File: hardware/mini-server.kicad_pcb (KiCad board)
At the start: 2 copper layers, 1 part

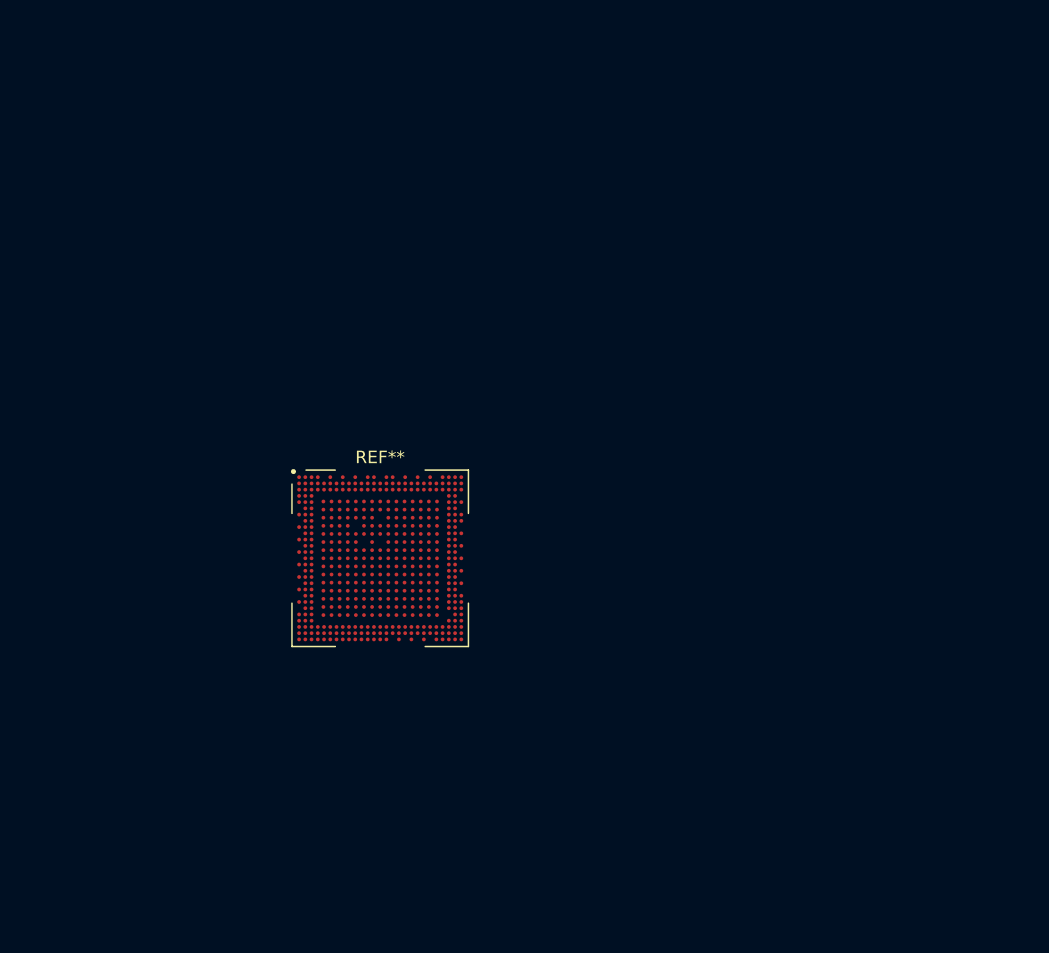
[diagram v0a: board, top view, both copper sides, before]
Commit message: Made a new power schematic and a new DDR4 ram schematic
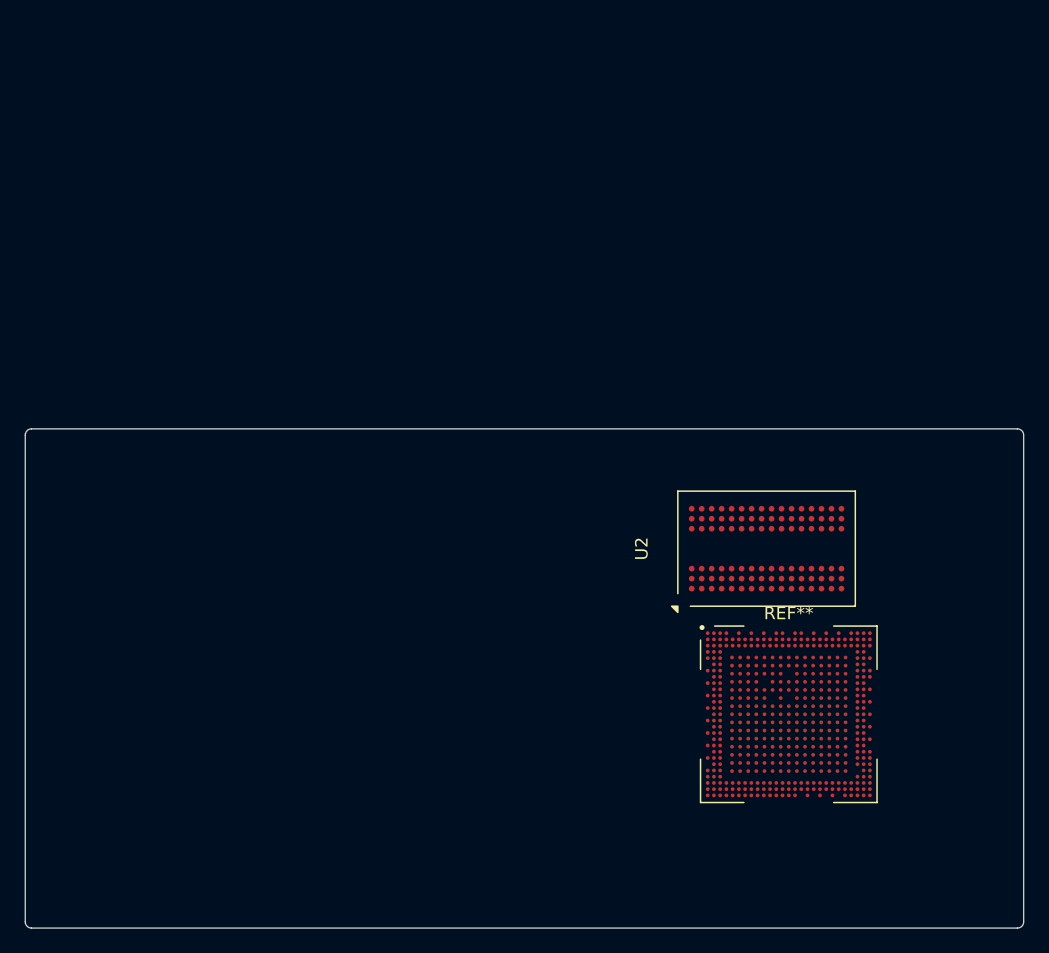
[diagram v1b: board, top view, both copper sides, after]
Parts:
- added U2: FJBD4N8GT6L9-SKC, easyeda2kicad:FBGA-96_L14.0-W9.0-R16-C6-P0.80-TL, F.Cu at (159.4, 89.1)
- U1: value ~ -> RK3562
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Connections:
- net Net-(U1-PMUPLL_AVSS) renamed GND
- U1 pad 1A1: (no net) -> unconnected-(U1D-DDR_DQS1P_A/DDR4_DQSU_P_A/LPDDR4_DQS1P_A/DDR3_DQS1P/LPDDR3_DQS1P-Pad1A1)
- U1 pad 1A10: (no net) -> unconnected-(U1D-AC4/DDR4_A4/LPDDR4_A3_B/DDR3_BA1-Pad1A10)
- U1 pad 1A13: (no net) -> unconnected-(U1D-DDR_DQS0P_B/DDR4_DQSU_P_B/LPDDR4_DQS0P_B/DDR3_DQS2P/LPDDR3_DQS2P-Pad1A13)
- U1 pad 1A15: (no net) -> unconnected-(U1D-DDR_DQS1P_B/DDR4_DQSL_P_B/LPDDR4_DQS1P_B/DDR3_DQS3P/LPDDR3_DQS0P-Pad1A15)
- U1 pad 1A3: (no net) -> unconnected-(U1D-DDR_DQS0P_A/DDR4_DQSL_P_A/LPDDR4_DQS0P_A/DDR3_DQS0P/LPDDR3_DQS3P-Pad1A3)
- U1 pad 1A6: (no net) -> unconnected-(U1D-AC12/DDR4_A12/LPDDR4_A3_A/DDR3_BA0-Pad1A6)
- U1 pad 1A7: (no net) -> unconnected-(U1D-AC16/DDR4_A16_RASN/LPDDR4_A5_A/DDR3_RASN-Pad1A7)
- U1 pad 1A8: (no net) -> unconnected-(U1D-AC5/DDR4_A5/LPDDR4_A5_B/DDR3_A11-Pad1A8)
- U1 pad 1A9: (no net) -> unconnected-(U1D-AC19/DDR4_BA1/LPDDR4_A4_B/DDR3_A12-Pad1A9)
- U1 pad 1B1: (no net) -> unconnected-(U1D-DDR_DQS1N_A/DDR4_DQSU_N_A/LPDDR4_DQS1N_A/DDR3_DQS1N/LPDDR3_DQS1N-Pad1B1)
- U1 pad 1B10: (no net) -> unconnected-(U1D-AC20/DDR4_BG0/LPDDR4_ODT1_CA_B/DDR3_WEN-Pad1B10)
- U1 pad 1B11: (no net) -> unconnected-(U1D-AC29/DDR4_RESETN/LPDDR4_RESETN/DDR3_RESETN-Pad1B11)
- U1 pad 1B13: (no net) -> unconnected-(U1D-DDR_DQS0N_B/DDR4_DQSU_N_B/LPDDR4_DQS0N_B/DDR3_DQS2N/LPDDR3_DQS2N-Pad1B13)
- U1 pad 1B15: (no net) -> unconnected-(U1D-DDR_DQS1N_B/DDR4_DQSL_N_B/LPDDR4_DQS1N_B/DDR3_DQS3N/LPDDR3_DQS0N-Pad1B15)
- U1 pad 1B3: (no net) -> unconnected-(U1D-DDR_DQS0N_A/DDR4_DQSL_N_A/LPDDR4_DQS0N_A/DDR3_DQS0N/LPDDR3_DQS3N-Pad1B3)
- U1 pad 1B6: (no net) -> unconnected-(U1D-AC1/DDR4_A1/DDR3_A2-Pad1B6)
- U1 pad 1B7: (no net) -> unconnected-(U1D-AC21/DDR4_BG1/LPDDR4_ODT1_CA_A/DDR3_BA2-Pad1B7)
- U1 pad 1B8: (no net) -> unconnected-(U1D-AC14/DDR4_A14_WEN/LPDDR4_A4_A/DDR3_A15-Pad1B8)
- U1 pad 1C9: (no net) -> unconnected-(U1D-DDR_VREFOUT-Pad1C9)
- U1 pad 1D11: (no net) -> +1V2
- U1 pad 1D4: (no net) -> unconnected-(U1D-DDR_RZQ-Pad1D4)
- U1 pad 1D6: (no net) -> +1V2
- U1 pad 1E1: (no net) -> unconnected-(U1A-SARADC1_IN7-Pad1E1)
- U1 pad 1E10: (no net) -> +1V2
- U1 pad 1E12: (no net) -> +0V9
- U1 pad 1E14: (no net) -> +1V8
- U1 pad 1E15: (no net) -> +1V8
- U1 pad 1E3: (no net) -> +1V2
- U1 pad 1E4: (no net) -> +1V2
- U1 pad 1E5: (no net) -> +1V2
- U1 pad 1E6: (no net) -> +1V2
- U1 pad 1E7: (no net) -> +1V2
- U1 pad 1E8: (no net) -> +1V2
- U1 pad 1E9: (no net) -> +1V2
- U1 pad 1F1: (no net) -> unconnected-(U1A-SARADC1_IN0-Pad1F1)
- U1 pad 1F11: (no net) -> +0V9
- U1 pad 1F12: (no net) -> +0V9
- U1 pad 1F13: (no net) -> +0V9
- U1 pad 1F14: (no net) -> unconnected-(U1E-VCCIO2-Pad1F14)
- U1 pad 1F2: (no net) -> unconnected-(U1A-SARADC1_IN2-Pad1F2)
- U1 pad 1G1: (no net) -> +1V8
- U1 pad 1G10: (no net) -> +0V9
- U1 pad 1G11: (no net) -> +0V9
- U1 pad 1G12: (no net) -> +0V9
- U1 pad 1G15: (no net) -> unconnected-(U1E-VCCIO3-Pad1G15)
- U1 pad 1G3: (no net) -> +0V9
- U1 pad 1G4: (no net) -> +0V9
- U1 pad 1G5: (no net) -> +0V9
- U1 pad 1G8: (no net) -> +0V9
- U1 pad 1H1: (no net) -> unconnected-(U1A-SARADC1_IN4-Pad1H1)
- U1 pad 1H10: (no net) -> +0V9
- U1 pad 1H11: (no net) -> +0V9
- U1 pad 1H14: (no net) -> unconnected-(U1E-VCCIO4-Pad1H14)
- U1 pad 1H15: (no net) -> unconnected-(U1C-I2S2_SDO_M0/RGMII_RXD1_M1/UART4_RTSN_M1/SPI2_MOSI_M1/PWM14_M1/RMII_RXD1/GPIO1_D7_d-Pad1H15)
- U1 pad 1H3: (no net) -> +0V9
- U1 pad 1H4: (no net) -> +0V9
- U1 pad 1H6: (no net) -> +0V9
- U1 pad 1H7: (no net) -> +0V9
- U1 pad 1H8: (no net) -> +0V9
- U1 pad 1J1: (no net) -> unconnected-(U1A-SARADC1_IN1-Pad1J1)
- U1 pad 1J10: (no net) -> +0V9
- U1 pad 1J11: (no net) -> +0V9
- U1 pad 1J12: (no net) -> +0V9
- U1 pad 1J14: (no net) -> unconnected-(U1B-SDMMC1_PWREN/RGMII_MDC_M1/PWM2_M1/I2C5_SCL_M1/RMII_MDC/GPIO1_C7_d-Pad1J14)
- U1 pad 1J15: (no net) -> unconnected-(U1C-I2S2_SDI_M0/RGMII_RXER_M1/UART4_CTSN_M1/SPI2_MISO_M1/PWM15_M1/RMII_RXER/GPIO2_A0_d-Pad1J15)
- U1 pad 1J2: (no net) -> unconnected-(U1A-SARADC1_IN3-Pad1J2)
- U1 pad 1J6: (no net) -> +0V9
- U1 pad 1J7: (no net) -> +0V9
- U1 pad 1K1: (no net) -> unconnected-(U1A-SARADC1_IN6-Pad1K1)
- U1 pad 1K10: (no net) -> +0V9
- U1 pad 1K14: (no net) -> +0V9
- U1 pad 1K15: (no net) -> +1V8
- U1 pad 1K2: (no net) -> +1V8
- U1 pad 1K3: (no net) -> unconnected-(U1E-VCCIO5-Pad1K3)
- U1 pad 1L1: (no net) -> unconnected-(U1C-I2C3_SDA_M0/UART2_RX_M1/SPDIF_TX_M0/UART5_RTSN_M1/GPIO3_A1_d-Pad1L1)
- U1 pad 1L11: (no net) -> +1V8
- U1 pad 1L12: (no net) -> unconnected-(U1A-PMUIO0-Pad1L12)
- U1 pad 1L13: (no net) -> +1V8
- U1 pad 1L14: (no net) -> +0V9
- U1 pad 1L2: (no net) -> unconnected-(U1A-SARADC1_IN5-Pad1L2)
- U1 pad 1L3: (no net) -> unconnected-(U1E-VCCIO1-Pad1L3)
- U1 pad 1L5: (no net) -> unconnected-(U1E-VCCIO6_2-Pad1L5)
- U1 pad 1L6: (no net) -> +0V9
- U1 pad 1L8: (no net) -> +0V9
- U1 pad 1M1: (no net) -> unconnected-(U1C-I2C3_SCL_M0/UART2_TX_M1/PDM_SDI3_M0/UART5_CTSN_M1/GPIO3_A0_d-Pad1M1)
- U1 pad 1M10: (no net) -> +0V9
- U1 pad 1M11: (no net) -> +0V9
- U1 pad 1M13: (no net) -> +0V9
- U1 pad 1M14: (no net) -> +3V3
- U1 pad 1M15: (no net) -> +1V8
- U1 pad 1M2: (no net) -> unconnected-(U1C-I2S0_SDO3_M0/I2S0_SDI1_M0/PDM_SDI1_M0/PCIE20_PERSTN_M1/GPIO3_B0_d-Pad1M2)
- U1 pad 1M4: (no net) -> unconnected-(U1E-VCCIO6_1-Pad1M4)
- U1 pad 1M7: (no net) -> +1V8
- U1 pad 1M8: (no net) -> +1V8
- U1 pad 1M9: (no net) -> +0V9
- U1 pad 1N9: (no net) -> +1V8
- U1 pad 1P12: (no net) -> unconnected-(U1A-nPOR-Pad1P12)
- U1 pad 1P14: (no net) -> unconnected-(U1A-USB30_OTG0_VBUSDET-Pad1P14)
- U1 pad 1P15: (no net) -> unconnected-(U1A-USB30_OTG0_ID-Pad1P15)
- U1 pad 1P3: (no net) -> unconnected-(U1C-MIPI_CSI_RX1_CLK1P-Pad1P3)
- U1 pad 1P7: (no net) -> unconnected-(U1C-MIPI_CSI_RX0_CLK1P-Pad1P7)
- U1 pad 1R11: (no net) -> unconnected-(U1A-UART2_RX_M0/PWM6_M0/NPU_AVS/GPIO0_C1_d-Pad1R11)
- U1 pad 1R13: (no net) -> unconnected-(U1A-TSADC_SHUT_M0/TSADC_SHUT_ORG/GPIO0_A1_z-Pad1R13)
- U1 pad 1R15: (no net) -> unconnected-(U1B-SDMMC0_DETN/I2C4_SDA_M1/GPIO0_A4_u-Pad1R15)
- U1 pad 1R3: (no net) -> unconnected-(U1C-MIPI_CSI_RX1_CLK1N-Pad1R3)
- U1 pad 1R7: (no net) -> unconnected-(U1C-MIPI_CSI_RX0_CLK1N-Pad1R7)
- U1 pad A10: (no net) -> unconnected-(U1D-AC2/DDR4_A2/LPDDR4_A1_A/DDR3_A4/LPDDR3_A6-PadA10)
- U1 pad A13: (no net) -> unconnected-(U1D-AC23/DDR4_CLK0P/LPDDR4_CLKN_A/DDR3_CLKP/LPDDR3_CLKP-PadA13)
- U1 pad A15: (no net) -> unconnected-(U1D-AC0/DDR4_A0/LPDDR4_CLKN_B/DDR3_A9-PadA15)
- U1 pad A18: (no net) -> unconnected-(U1D-AC6/DDR4_A6/LPDDR4_A1_B/DDR3_A14/LPDDR3_A1-PadA18)
- U1 pad A2: (no net) -> unconnected-(U1D-DDR_DM1_A/DDR4_DMU_A/LPDDR4_DM1_A/DDR3_DM1/LPDDR3_DM1-PadA2)
- U1 pad A20: (no net) -> unconnected-(U1D-DDR_DQ2_B/DDR4_DQU1_B/LPDDR4_DQ2_B/DDR3_DQ22/LPDDR3_DQ16-PadA20)
- U1 pad A22: (no net) -> unconnected-(U1D-DDR_DQ7_B/DDR4_DQU6_B/LPDDR4_DQ7_B/DDR3_DQ17/LPDDR3_DQ22-PadA22)
- U1 pad A24: (no net) -> unconnected-(U1D-DDR_DQ12_B/DDR4_DQL5_B/LPDDR4_DQ12_B/DDR3_DQ25/LPDDR3_DQ3-PadA24)
- U1 pad A25: (no net) -> unconnected-(U1D-DDR_DQ14_B/DDR4_DQL1_B/LPDDR4_DQ14_B/DDR3_DQ27/LPDDR3_DQ4-PadA25)
- U1 pad A26: (no net) -> unconnected-(U1D-DDR_DM1_B/DDR4_DML_B/LPDDR4_DM1_B/DDR3_DM3/LPDDR3_DM0-PadA26)
- U1 pad A3: (no net) -> /DDR4_PHY/DQU2
- U1 pad A4: (no net) -> /DDR4_PHY/DQU0
- U1 pad A6: (no net) -> /DDR4_PHY/DQL7
- U1 pad A8: (no net) -> /DDR4_PHY/DQL0
- U1 pad AA1: (no net) -> unconnected-(U1B-VO_LCDC_D22/RGMII_TXD0_M0/UART6_CTSN_M1/SPI1_MOSI_M0/GPIO4_A2_d-PadAA1)
- U1 pad AA2: (no net) -> unconnected-(U1B-VO_LCDC_D23/RGMII_TXD1_M0/UART6_RTSN_M1/SPI1_MISO_M0/GPIO4_A3_d-PadAA2)
- U1 pad AA25: (no net) -> unconnected-(U1A-UART1_RTSN_M0/RGMII_TXEN_M1/I2S0_SDI2_M1/PWM6_M1/RMII_TXEN/GPIO1_D3_d-PadAA25)
- U1 pad AA3: (no net) -> unconnected-(U1B-VO_LCDC_D0/RGMII_TXEN_M0/PWM13_M0/GPIO4_A4_d-PadAA3)
- U1 pad AB2: (no net) -> unconnected-(U1B-VO_LCDC_D14/RGMII_TXD3_M0/UART8_RX_M1/I2S2_SDO_M1/GPIO3_D5_d-PadAB2)
- U1 pad AB26: (no net) -> unconnected-(U1A-USB30_OTG0_SSRXP/PCIE20_RXDP-PadAB26)
- U1 pad AB27: (no net) -> unconnected-(U1A-USB30_OTG0_SSRXN/PCIE20_RXDN-PadAB27)
- U1 pad AB3: (no net) -> unconnected-(U1B-VO_LCDC_D13/RGMII_TXD2_M0/UART8_TX_M1/I2S2_SDI_M1/GPIO3_D4_d-PadAB3)
- U1 pad AC1: (no net) -> unconnected-(U1B-VO_LCDC_D2/RGMII_MDC_M0/UART9_TX_M0/GPIO4_B2_d-PadAC1)
- U1 pad AC2: (no net) -> unconnected-(U1B-VO_LCDC_D18/RGMII_MDIO_M0/UART9_RX_M0/GPIO4_B3_d-PadAC2)
- U1 pad AC26: (no net) -> unconnected-(U1A-PCIE20_REFCLKP-PadAC26)
- U1 pad AC27: (no net) -> unconnected-(U1A-PCIE20_REFCLKN-PadAC27)
- U1 pad AD1: (no net) -> unconnected-(U1C-MIPI_CSI_RX1_D3P-PadAD1)
- U1 pad AD2: (no net) -> unconnected-(U1C-MIPI_CSI_RX1_D3N-PadAD2)
- U1 pad AD26: (no net) -> unconnected-(U1A-USB30_OTG0_SSTXP/PCIE20_TXDP-PadAD26)
- U1 pad AD27: (no net) -> unconnected-(U1A-USB30_OTG0_SSTXN/PCIE20_TXDN-PadAD27)
- U1 pad AE1: (no net) -> unconnected-(U1C-MIPI_CSI_RX1_D2P-PadAE1)
- U1 pad AE15: (no net) -> unconnected-(U1C-I2C2_SDA_M0/PCIE20_WAKEN_M0/GPIO0_B6_d-PadAE15)
- U1 pad AE16: (no net) -> unconnected-(U1A-UART2_RTSN_M0/PWM0_M0/SPI0_CLK_M0/GPIO0_C3_d-PadAE16)
- U1 pad AE17: (no net) -> unconnected-(U1C-I2C1_SCL_M0/GPIO0_B3_d-PadAE17)
- U1 pad AE18: (no net) -> unconnected-(U1A-UART6_RTSN_M0/PWM2_M0/SPI0_MISO_M0/GPIO0_C5_d-PadAE18)
- U1 pad AE19: (no net) -> unconnected-(U1A-UART6_RX_M0/GPIO0_C7_d-PadAE19)
- U1 pad AE20: (no net) -> unconnected-(U1A-UART0_TX_M0/JTAG_CPU_MCU_TCK_M0/GPIO0_D1_u-PadAE20)
- U1 pad AE22: (no net) -> unconnected-(U1B-SDMMC0_PWREN/I2C4_SCL_M1/PMU_DEBUG/GPIO0_A5_d-PadAE22)
- U1 pad AE23: (no net) -> unconnected-(U1C-I2C0_SDA/GPIO0_B2_d-PadAE23)
- U1 pad AE24: (no net) -> unconnected-(U1A-REF_CLK_OUT/GPIO0_A0_d-PadAE24)
- U1 pad AE26: (no net) -> unconnected-(U1A-USB20_HOST1_DM-PadAE26)
- U1 pad AE27: (no net) -> unconnected-(U1A-USB20_HOST1_DP-PadAE27)
- U1 pad AF1: (no net) -> unconnected-(U1C-MIPI_CSI_RX1_D2N-PadAF1)
- U1 pad AF10: (no net) -> unconnected-(U1C-MIPI_DSI_TX_D3N/LVDS_TX_D3N-PadAF10)
- U1 pad AF11: (no net) -> unconnected-(U1C-MIPI_DSI_TX_D2P/LVDS_TX_D2P-PadAF11)
- U1 pad AF12: (no net) -> unconnected-(U1C-MIPI_DSI_TX_CLKN/LVDS_TX_CLKN-PadAF12)
- U1 pad AF13: (no net) -> unconnected-(U1C-MIPI_DSI_TX_D1P/LVDS_TX_D1P-PadAF13)
- U1 pad AF14: (no net) -> unconnected-(U1C-MIPI_DSI_TX_D0N/LVDS_TX_D0N-PadAF14)
- U1 pad AF15: (no net) -> unconnected-(U1A-SPI0_CSN1_M0/PWM4_M0/CPU_AVS/SPDIF_TX_M1/GPIO0_B7_d-PadAF15)
- U1 pad AF16: (no net) -> unconnected-(U1C-I2C2_SCL_M0/PCIE20_PERSTN_M0/GPIO0_B5_d-PadAF16)
- U1 pad AF17: (no net) -> unconnected-(U1A-UART2_TX_M0/PWM7_M0/GPU_AVS/GPIO0_C0_d-PadAF17)
- U1 pad AF18: (no net) -> unconnected-(U1C-I2C1_SDA_M0/GPIO0_B4_d-PadAF18)
- U1 pad AF19: (no net) -> unconnected-(U1A-UART6_TX_M0/GPIO0_C6_d-PadAF19)
- U1 pad AF2: (no net) -> unconnected-(U1C-MIPI_CSI_RX1_CLK0P-PadAF2)
- U1 pad AF20: (no net) -> unconnected-(U1A-UART0_RX_M0/JTAG_CPU_MCU_TMS_M0/GPIO0_D0_u-PadAF20)
- U1 pad AF21: (no net) -> unconnected-(U1A-CLK_32K_IN/CLK0_32K_OUT/PCIE20_BUTTONRSTN/GPIO0_B0_d-PadAF21)
- U1 pad AF22: (no net) -> unconnected-(U1A-PWR_CTRL1/GPIO0_A3_u-PadAF22)
- U1 pad AF23: (no net) -> unconnected-(U1A-PWR_CTRL0/TSADC_SHUT_M1/GPIO0_A2_d-PadAF23)
- U1 pad AF25: (no net) -> unconnected-(U1A-OSC_SOC_XOUT-PadAF25)
- U1 pad AF26: (no net) -> unconnected-(U1A-USB30_OTG0_DM-PadAF26)
- U1 pad AF27: (no net) -> unconnected-(U1A-USB30_OTG0_DP-PadAF27)
- U1 pad AF3: (no net) -> unconnected-(U1C-MIPI_CSI_RX1_D1P-PadAF3)
- U1 pad AF4: (no net) -> unconnected-(U1C-MIPI_CSI_RX1_D0P-PadAF4)
- U1 pad AF5: (no net) -> unconnected-(U1C-MIPI_CSI_RX0_D3P-PadAF5)
- U1 pad AF6: (no net) -> unconnected-(U1C-MIPI_CSI_RX0_D2P-PadAF6)
- U1 pad AF7: (no net) -> unconnected-(U1C-MIPI_CSI_RX0_CLK0P-PadAF7)
- U1 pad AF8: (no net) -> unconnected-(U1C-MIPI_CSI_RX0_D1P-PadAF8)
- U1 pad AF9: (no net) -> unconnected-(U1C-MIPI_CSI_RX0_D0P-PadAF9)
- U1 pad AG10: (no net) -> unconnected-(U1C-MIPI_DSI_TX_D3P/LVDS_TX_D3P-PadAG10)
- U1 pad AG11: (no net) -> unconnected-(U1C-MIPI_DSI_TX_D2N/LVDS_TX_D2N-PadAG11)
- U1 pad AG12: (no net) -> unconnected-(U1C-MIPI_DSI_TX_CLKP/LVDS_TX_CLKP-PadAG12)
- U1 pad AG13: (no net) -> unconnected-(U1C-MIPI_DSI_TX_D1N/LVDS_TX_D1N-PadAG13)
- U1 pad AG14: (no net) -> unconnected-(U1C-MIPI_DSI_TX_D0P/LVDS_TX_D0P-PadAG14)
- U1 pad AG17: (no net) -> unconnected-(U1A-UART2_CTSN_M0/PWM5_M0/SPI0_CSN0_M0/GPIO0_C2_d-PadAG17)
- U1 pad AG19: (no net) -> unconnected-(U1A-UART6_CTSN_M0/PWM1_M0/SPI0_MOSI_M0/GPIO0_C4_d-PadAG19)
- U1 pad AG2: (no net) -> unconnected-(U1C-MIPI_CSI_RX1_CLK0N-PadAG2)
- U1 pad AG21: (no net) -> unconnected-(U1A-PWM3_M0/GPIO0_A7_d-PadAG21)
- U1 pad AG23: (no net) -> unconnected-(U1C-I2C0_SCL/GPIO0_B1_d-PadAG23)
- U1 pad AG24: (no net) -> unconnected-(U1A-PCIE20_CLKREQN_M0/GPIO0_A6_d-PadAG24)
- U1 pad AG25: (no net) -> unconnected-(U1A-OSC_SOC_XIN-PadAG25)
- U1 pad AG3: (no net) -> unconnected-(U1C-MIPI_CSI_RX1_D1N-PadAG3)
- U1 pad AG4: (no net) -> unconnected-(U1C-MIPI_CSI_RX1_D0N-PadAG4)
- U1 pad AG5: (no net) -> unconnected-(U1C-MIPI_CSI_RX0_D3N-PadAG5)
- U1 pad AG6: (no net) -> unconnected-(U1C-MIPI_CSI_RX0_D2N-PadAG6)
- U1 pad AG7: (no net) -> unconnected-(U1C-MIPI_CSI_RX0_CLK0N-PadAG7)
- U1 pad AG8: (no net) -> unconnected-(U1C-MIPI_CSI_RX0_D1N-PadAG8)
- U1 pad AG9: (no net) -> unconnected-(U1C-MIPI_CSI_RX0_D0N-PadAG9)
- U1 pad B1: (no net) -> /DDR4_PHY/DQU3
- U1 pad B10: (no net) -> unconnected-(U1D-AC11/DDR4_A11/LPDDR4_A0_A/DDR3_A6/LPDDR3_A8-PadB10)
- U1 pad B11: (no net) -> unconnected-(U1D-AC3/DDR4_A3/LPDDR4_CS0N_A/DDR3_ODT1/LPDDR3_ODT0-PadB11)
- U1 pad B12: (no net) -> unconnected-(U1D-AC25/DDR4_CS0N/LPDDR4_CKE1_A/DDR3_A3-PadB12)
- U1 pad B13: (no net) -> unconnected-(U1D-AC24/DDR4_CLK0N/LPDDR4_CLKP_A/DDR3_CLKN/LPDDR3_CLKN-PadB13)
- U1 pad B15: (no net) -> unconnected-(U1D-AC9/DDR4_A9/LPDDR4_CLKP_B/DDR3_A13-PadB15)
- U1 pad B16: (no net) -> unconnected-(U1D-AC17/DDR4_ACTN/LPDDR4_CKE1_B/DDR3_CASN/LPDDR3_CS1N-PadB16)
- U1 pad B17: (no net) -> unconnected-(U1D-AC28/DDR4_ODT1/LPDDR4_CS0N_B/DDR3_CS0N/LPDDR3_A2-PadB17)
- U1 pad B18: (no net) -> unconnected-(U1D-AC7/DDR4_A7/LPDDR4_A0_B/DDR3_A5/LPDDR3_A0-PadB18)
- U1 pad B19: (no net) -> unconnected-(U1D-AC13/DDR4_A13/LPDDR4_ODT0_CA_B/DDR3_A8/LPDDR3_ODT1-PadB19)
- U1 pad B2: (no net) -> /DDR4_PHY/DQU7
- U1 pad B20: (no net) -> unconnected-(U1D-DDR_DQ1_B/DDR4_DQU3_B/LPDDR4_DQ1_B/DDR3_DQ20/LPDDR3_DQ21-PadB20)
- U1 pad B21: (no net) -> unconnected-(U1D-DDR_DM0_B/DDR4_DMU_B/LPDDR4_DM0_B/DDR3_DM2/LPDDR3_DM2-PadB21)
- U1 pad B22: (no net) -> unconnected-(U1D-DDR_DQ0_B/DDR4_DQU7_B/LPDDR4_DQ0_B/DDR3_DQ16/LPDDR3_DQ17-PadB22)
- U1 pad B23: (no net) -> unconnected-(U1D-DDR_DQ5_B/DDR4_DQU4_B/LPDDR4_DQ5_B/DDR3_DQ23/LPDDR3_DQ19-PadB23)
- U1 pad B24: (no net) -> unconnected-(U1D-DDR_DQ13_B/DDR4_DQL7_B/LPDDR4_DQ13_B/DDR3_DQ31/LPDDR3_DQ5-PadB24)
- U1 pad B25: (no net) -> unconnected-(U1D-DDR_DQ15_B/DDR4_DQL3_B/LPDDR4_DQ15_B/DDR3_DQ29/LPDDR3_DQ7-PadB25)
- U1 pad B26: (no net) -> unconnected-(U1D-DDR_DQ11_B/DDR4_DQL6_B/LPDDR4_DQ11_B/DDR3_DQ24/LPDDR3_DQ6-PadB26)
- U1 pad B27: (no net) -> unconnected-(U1D-DDR_DQ10_B/DDR4_DQL2_B/LPDDR4_DQ10_B/DDR3_DQ28/LPDDR3_DQ2-PadB27)
- U1 pad B3: (no net) -> /DDR4_PHY/DQU6
- U1 pad B4: (no net) -> /DDR4_PHY/DQU4
- U1 pad B5: (no net) -> /DDR4_PHY/DQL1
- U1 pad B6: (no net) -> /DDR4_PHY/DQL6
- U1 pad B7: (no net) -> unconnected-(U1D-DDR_DM0_A/DDR4_DML_A/LPDDR4_DM0_A/DDR3_DM0/LPDDR3_DM3-PadB7)
- U1 pad B8: (no net) -> /DDR4_PHY/DQL2
- U1 pad B9: (no net) -> unconnected-(U1D-AC8/DDR4_A8/LPDDR4_ODT0_CA_A/DDR3_A7/LPDDR3_A9-PadB9)
- U1 pad C1: (no net) -> /DDR4_PHY/DQU5
- U1 pad C10: (no net) -> unconnected-(U1D-AC15/DDR4_A15_CASN/LPDDR4_A2_A/DDR3_A0/LPDDR3_A7-PadC10)
- U1 pad C11: (no net) -> unconnected-(U1D-AC26/DDR4_CS1N/LPDDR4_CS1N_A/DDR3_CS1N/LPDDR3_A5-PadC11)
- U1 pad C12: (no net) -> unconnected-(U1D-AC22/DDR4_CKE0/LPDDR4_CKE0_A/DDR3_CKE/LPDDR3_CKE-PadC12)
- U1 pad C16: (no net) -> unconnected-(U1D-AC10/DDR4_A10/LPDDR4_CKE0_B/DDR3_A10/LPDDR3_CS0N-PadC16)
- U1 pad C17: (no net) -> unconnected-(U1D-AC27/DDR4_ODT0/LPDDR4_CS1N_B/DDR3_ODT0/LPDDR3_A4-PadC17)
- U1 pad C18: (no net) -> unconnected-(U1D-AC18/DDR4_BA0/LPDDR4_A2_B/DDR3_A1/LPDDR3_A3-PadC18)
- U1 pad C2: (no net) -> /DDR4_PHY/DQU1
- U1 pad C20: (no net) -> unconnected-(U1D-DDR_DQ3_B/DDR4_DQU5_B/LPDDR4_DQ3_B/DDR3_DQ18/LPDDR3_DQ20-PadC20)
- U1 pad C22: (no net) -> unconnected-(U1D-DDR_DQ6_B/DDR4_DQU2_B/LPDDR4_DQ6_B/DDR3_DQ19/LPDDR3_DQ18-PadC22)
- U1 pad C23: (no net) -> unconnected-(U1D-DDR_DQ4_B/DDR4_DQU0_B/LPDDR4_DQ4_B/DDR3_DQ21/LPDDR3_DQ23-PadC23)
- U1 pad C26: (no net) -> unconnected-(U1D-DDR_DQ8_B/DDR4_DQL0_B/LPDDR4_DQ8_B/DDR3_DQ26/LPDDR3_DQ0-PadC26)
- U1 pad C27: (no net) -> unconnected-(U1D-DDR_DQ9_B/DDR4_DQL4_B/LPDDR4_DQ9_B/DDR3_DQ30/LPDDR3_DQ1-PadC27)
- U1 pad C5: (no net) -> /DDR4_PHY/DQL5
- U1 pad C6: (no net) -> /DDR4_PHY/DQL3
- U1 pad C8: (no net) -> /DDR4_PHY/DQL4
- U1 pad D1: (no net) -> unconnected-(U1C-I2S1_SDO0_M1/CAM_CLK3_OUT/UART8_RTSN_M0/SPI0_CLK_M1/PWM13_M1/GPIO3_B5_d-PadD1)
- U1 pad D25: (no net) -> unconnected-(U1A-SARADC0_IN4-PadD25)
- U1 pad D26: (no net) -> unconnected-(U1A-SARADC0_BOOT-PadD26)
- U1 pad D3: (no net) -> unconnected-(U1C-I2C5_SDA_M0/ISP_FLASH_TRIGOUT/UART9_RX_M1/GPIO3_C3_d-PadD3)
- U1 pad E1: (no net) -> unconnected-(U1C-I2C5_SCL_M0/ISP_PRELIGHT_TRIGOUT/UART9_TX_M1/GPIO3_C2_d-PadE1)
- U1 pad E2: (no net) -> unconnected-(U1C-I2S1_SDI0_M1/ISP_FLASH_TRIGIN/UART3_RTSN_M1/GPIO3_C1_d-PadE2)
- U1 pad E25: (no net) -> unconnected-(U1A-SARADC0_IN2-PadE25)
- U1 pad E26: (no net) -> unconnected-(U1A-SARADC0_IN5-PadE26)
- U1 pad E27: (no net) -> unconnected-(U1A-SARADC0_IN6-PadE27)
- U1 pad F2: (no net) -> unconnected-(U1C-I2S1_LRCK_M1/CAM_CLK2_OUT/UART8_CTSN_M0/SPI0_MOSI_M1/PWM12_M1/GPIO3_B4_d-PadF2)
- U1 pad F25: (no net) -> unconnected-(U1A-SARADC0_IN7-PadF25)
- U1 pad F26: (no net) -> unconnected-(U1A-SARADC0_IN1-PadF26)
- U1 pad G1: (no net) -> unconnected-(U1C-I2S1_SCLK_M1/CAM_CLK1_OUT_M0/UART8_RX_M0/GPIO3_B3_d-PadG1)
- U1 pad G2: (no net) -> unconnected-(U1C-I2S1_SDO2_M1/I2S1_SDI2_M1/UART3_TX_M1/SPI0_CSN0_M1/I2C4_SDA_M0/GPIO3_B7_d-PadG2)
- U1 pad G26: (no net) -> unconnected-(U1A-SARADC0_IN3-PadG26)
- U1 pad G3: (no net) -> unconnected-(U1C-I2S1_SDO1_M1/I2S1_SDI3_M1/UART3_CTSN_M1/SPI0_CSN1_M1/I2C4_SCL_M0/GPIO3_B6_d-PadG3)
- U1 pad H2: (no net) -> unconnected-(U1C-I2S1_SDO3_M1/I2S1_SDI1_M1/UART3_RX_M1/SPI0_MISO_M1/GPIO3_C0_d-PadH2)
- U1 pad H25: (no net) -> unconnected-(U1A-EMMC_D2/FSPI_D2/GPIO1_A2_u-PadH25)
- U1 pad H26: (no net) -> unconnected-(U1A-EMMC_D6/GPIO1_A6_u-PadH26)
- U1 pad H27: (no net) -> unconnected-(U1A-EMMC_D7/GPIO1_A7_u-PadH27)
- U1 pad H3: (no net) -> unconnected-(U1C-I2S1_MCLK_M1/CAM_CLK0_OUT_M0/UART8_TX_M0/GPIO3_B2_d-PadH3)
- U1 pad J1: (no net) -> unconnected-(U1C-I2S0_SDO1_M0/I2S0_SDI3_M0/PDM_CLK0_M0/PCIE20_CLKREQN_M1/UART5_TX_M1/GPIO3_A6_d-PadJ1)
- U1 pad J2: (no net) -> unconnected-(U1C-I2S0_SDI0_M0/PDM_SDI0_M0/GPIO3_B1_d-PadJ2)
- U1 pad J25: (no net) -> unconnected-(U1A-EMMC_D0/FSPI_D0/GPIO1_A0_u-PadJ25)
- U1 pad J26: (no net) -> unconnected-(U1A-EMMC_D1/FSPI_D1/GPIO1_A1_u-PadJ26)
- U1 pad K2: (no net) -> unconnected-(U1C-I2S0_MCLK_M0/UART2_CTSN_M1/PDM_CLK1_M0/GPIO3_A2_d-PadK2)
- U1 pad K25: (no net) -> unconnected-(U1A-EMMC_D5/GPIO1_A5_u-PadK25)
- U1 pad K26: (no net) -> unconnected-(U1A-EMMC_D4/GPIO1_A4_u-PadK26)
- U1 pad K27: (no net) -> unconnected-(U1A-EMMC_D3/FSPI_D3/GPIO1_A3_u-PadK27)
- U1 pad K3: (no net) -> unconnected-(U1C-I2S0_SDO0_M0/PWM9_M0/GPIO3_A5_d-PadK3)
- U1 pad L1: (no net) -> unconnected-(U1C-I2S0_LRCK_M0/PWM8_M0/GPIO3_A4_d-PadL1)
- U1 pad L2: (no net) -> unconnected-(U1C-I2S0_SDO2_M0/I2S0_SDI2_M0/PDM_SDI2_M0/PCIE20_WAKEN_M1/UART5_RX_M1/GPIO3_A7_d-PadL2)
- U1 pad L26: (no net) -> unconnected-(U1A-EMMC_STRB/FSPI_CSN1/GPIO1_B2_d-PadL26)
- U1 pad L3: (no net) -> unconnected-(U1C-I2S0_SCLK_M0/UART2_RTSN_M1/GPIO3_A3_d-PadL3)
- U1 pad M2: (no net) -> unconnected-(U1B-VO_LCDC_HSYNC/I2S1_SDO1_M0/UART9_CTSN_M0/SPI2_CSN1_M0/I2C1_SCL_M1/UART3_TX_M0/GPIO4_B4_d-PadM2)
- U1 pad M25: (no net) -> unconnected-(U1A-EMMC_CLK/FSPI_CLK/GPIO1_B1_d-PadM25)
- U1 pad M26: (no net) -> unconnected-(U1A-EMMC_CMD/FSPI_CSN0/GPIO1_B0_u-PadM26)
- U1 pad M3: (no net) -> unconnected-(U1B-VO_LCDC_VSYNC/I2S1_SDO2_M0/UART9_RTSN_M0/SPI2_CSN0_M0/I2C1_SDA_M1/UART3_RX_M0/GPIO4_B5_d-PadM3)
- U1 pad N1: (no net) -> unconnected-(U1B-VO_LCDC_D3/I2S1_MCLK_M0/UART7_TX_M0/GPIO3_C4_d-PadN1)
- U1 pad N2: (no net) -> unconnected-(U1B-VO_LCDC_D4/I2S1_SCLK_M0/UART4_CTSN_M0/PWM14_M0/GPIO3_C5_d-PadN2)
- U1 pad N25: (no net) -> unconnected-(U1B-SDMMC0_D2/JTAG_CPU_MCU_TCK_M1/UART5_CTSN_M0/SPI1_CSN1_M1/PWM10_M0/DSM_AUD_RP/GPIO1_B5_u-PadN25)
- U1 pad N26: (no net) -> unconnected-(U1B-SDMMC0_D3/JTAG_CPU_MCU_TMS_M1/UART5_RTSN_M0/SPI1_CSN0_M1/PWM11_M0/DSM_AUD_RN/GPIO1_B6_u-PadN26)
- U1 pad N3: (no net) -> unconnected-(U1B-VO_LCDC_DEN/I2S1_SDO3_M0/UART3_CTSN_M0/SPI2_CLK_M0/GPIO4_B6_d-PadN3)
- U1 pad P2: (no net) -> unconnected-(U1B-VO_LCDC_D6/I2S1_SDO0_M0/UART7_RX_M0/GPIO3_C7_d-PadP2)
- U1 pad P25: (no net) -> unconnected-(U1B-SDMMC0_CMD/SPDIF_TX_M2/UART5_RX_M0/GPIO1_B7_u-PadP25)
- U1 pad P27: (no net) -> unconnected-(U1B-SDMMC0_CLK/TEST_CLK_OUT/UART5_TX_M0/SPI1_CLK_M1/GPIO1_C0_d-PadP27)
- U1 pad P3: (no net) -> unconnected-(U1B-VO_LCDC_D5/I2S1_LRCK_M0/UART4_RTSN_M0/PWM15_M0/GPIO3_C6_d-PadP3)
- U1 pad R1: (no net) -> unconnected-(U1B-VO_LCDC_D10/I2S1_SDI1_M0/UART4_RX_M0/UART3_RTSN_M0/GPIO3_D1_d-PadR1)
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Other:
- board outline added: 80 x 40 mm

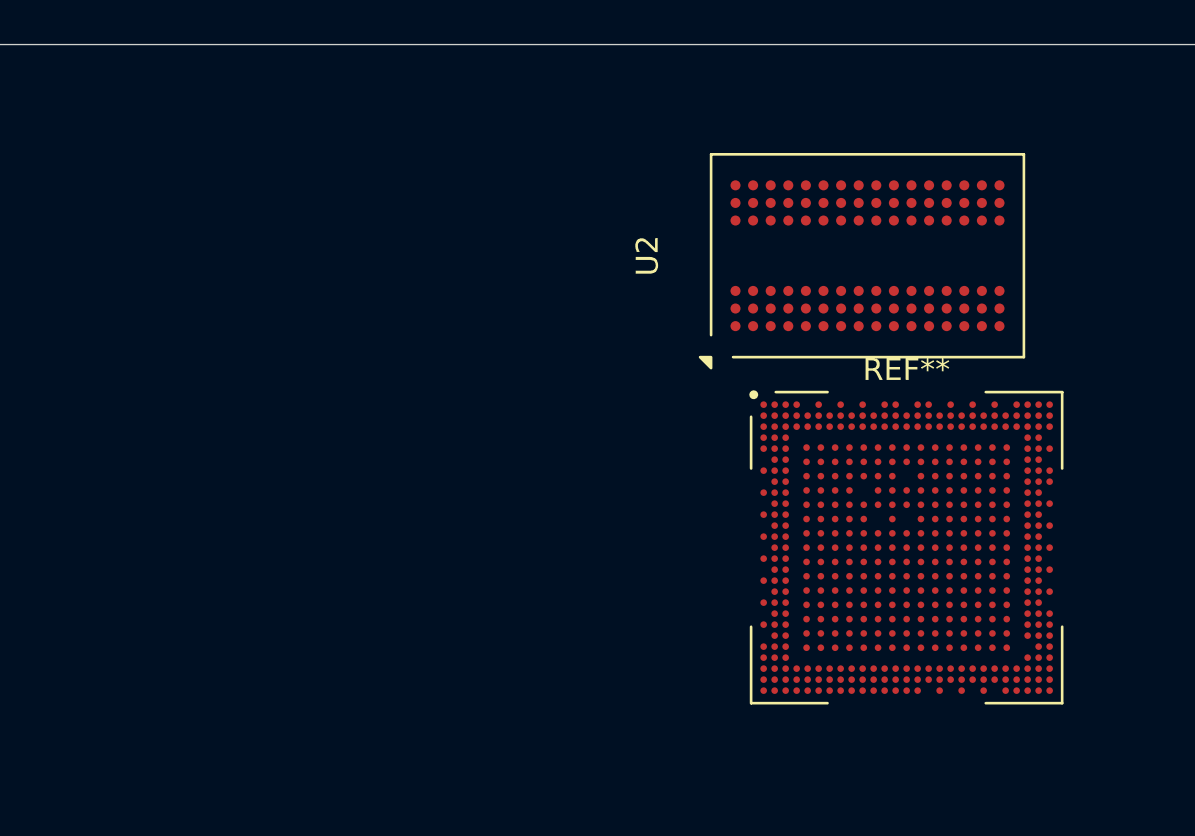
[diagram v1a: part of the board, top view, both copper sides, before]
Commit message: DDR4 schematic almost completed
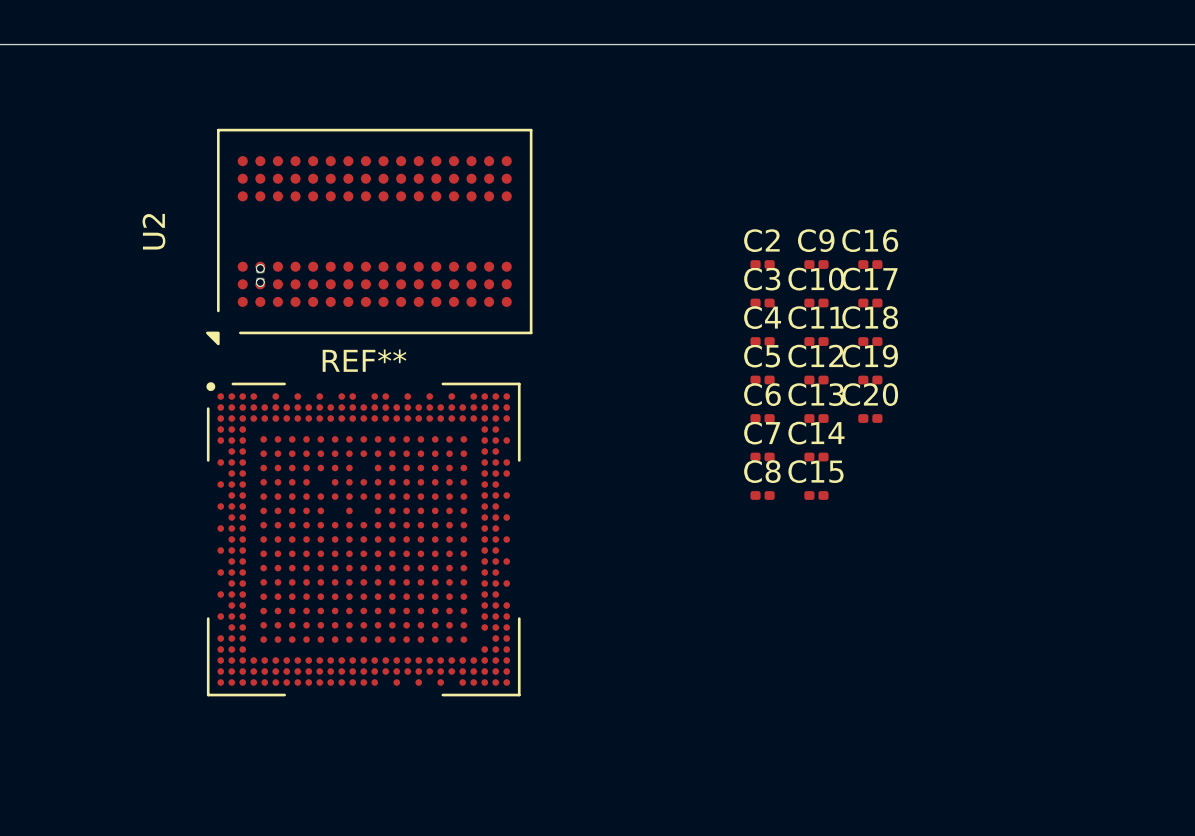
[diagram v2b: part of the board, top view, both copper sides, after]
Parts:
- added C1: 100n, Capacitor_SMD:C_0201_0603Metric, B.Cu at (131.8, 90.0)
- added C10: 100n, Capacitor_SMD:C_0201_0603Metric, F.Cu at (157.1, 91.2)
- added C11: 100n, Capacitor_SMD:C_0201_0603Metric, F.Cu at (157.1, 93.0)
- added C12: 100n, Capacitor_SMD:C_0201_0603Metric, F.Cu at (157.1, 94.8)
- added C13: 100n, Capacitor_SMD:C_0201_0603Metric, F.Cu at (157.1, 96.5)
- added C14: 100n, Capacitor_SMD:C_0201_0603Metric, F.Cu at (157.1, 98.2)
- added C15: 100n, Capacitor_SMD:C_0201_0603Metric, F.Cu at (157.1, 100.0)
- added C16: 100n, Capacitor_SMD:C_0201_0603Metric, F.Cu at (159.5, 89.5)
- added C17: 100n, Capacitor_SMD:C_0201_0603Metric, F.Cu at (159.5, 91.2)
- added C18: 100n, Capacitor_SMD:C_0201_0603Metric, F.Cu at (159.5, 93.0)
- added C19: 100n, Capacitor_SMD:C_0201_0603Metric, F.Cu at (159.5, 94.8)
- added C2: 100n, Capacitor_SMD:C_0201_0603Metric, F.Cu at (154.6, 89.5)
- added C20: 100n, Capacitor_SMD:C_0201_0603Metric, F.Cu at (159.5, 96.5)
- added C3: 100n, Capacitor_SMD:C_0201_0603Metric, F.Cu at (154.6, 91.2)
- added C4: 100n, Capacitor_SMD:C_0201_0603Metric, F.Cu at (154.6, 93.0)
- added C5: 100n, Capacitor_SMD:C_0201_0603Metric, F.Cu at (154.6, 94.8)
- added C6: 100n, Capacitor_SMD:C_0201_0603Metric, F.Cu at (154.6, 96.5)
- added C7: 100n, Capacitor_SMD:C_0201_0603Metric, F.Cu at (154.6, 98.2)
- added C8: 100n, Capacitor_SMD:C_0201_0603Metric, F.Cu at (154.6, 100.0)
- added C9: 100n, Capacitor_SMD:C_0201_0603Metric, F.Cu at (157.1, 89.5)
- moved U1 24.7 mm to (136.5, 102.0)
- moved U2 22.4 mm to (137.0, 88.0)
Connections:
- U1 pad 1A1: unconnected-(U1D-DDR_DQS1P_A/DDR4_DQSU_P_A/LPDDR4_DQS1P_A/DDR3_DQS1P/LPDDR3_DQS1P-Pad1A1) -> /RK3562_CORE/DQSU_t
- U1 pad 1A10: unconnected-(U1D-AC4/DDR4_A4/LPDDR4_A3_B/DDR3_BA1-Pad1A10) -> /RK3562_CORE/A4
- U1 pad 1A3: unconnected-(U1D-DDR_DQS0P_A/DDR4_DQSL_P_A/LPDDR4_DQS0P_A/DDR3_DQS0P/LPDDR3_DQS3P-Pad1A3) -> /RK3562_CORE/DQSL_t
- U1 pad 1A6: unconnected-(U1D-AC12/DDR4_A12/LPDDR4_A3_A/DDR3_BA0-Pad1A6) -> /RK3562_CORE/A12
- U1 pad 1A7: unconnected-(U1D-AC16/DDR4_A16_RASN/LPDDR4_A5_A/DDR3_RASN-Pad1A7) -> /RK3562_CORE/RAS_n
- U1 pad 1A8: unconnected-(U1D-AC5/DDR4_A5/LPDDR4_A5_B/DDR3_A11-Pad1A8) -> /RK3562_CORE/A5
- U1 pad 1A9: unconnected-(U1D-AC19/DDR4_BA1/LPDDR4_A4_B/DDR3_A12-Pad1A9) -> /RK3562_CORE/BA1
- U1 pad 1B1: unconnected-(U1D-DDR_DQS1N_A/DDR4_DQSU_N_A/LPDDR4_DQS1N_A/DDR3_DQS1N/LPDDR3_DQS1N-Pad1B1) -> /RK3562_CORE/DQSU_c
- U1 pad 1B10: unconnected-(U1D-AC20/DDR4_BG0/LPDDR4_ODT1_CA_B/DDR3_WEN-Pad1B10) -> /RK3562_CORE/BG0
- U1 pad 1B11: unconnected-(U1D-AC29/DDR4_RESETN/LPDDR4_RESETN/DDR3_RESETN-Pad1B11) -> /RK3562_CORE/RESET_n
- U1 pad 1B3: unconnected-(U1D-DDR_DQS0N_A/DDR4_DQSL_N_A/LPDDR4_DQS0N_A/DDR3_DQS0N/LPDDR3_DQS3N-Pad1B3) -> /RK3562_CORE/DQSL_c
- U1 pad 1B6: unconnected-(U1D-AC1/DDR4_A1/DDR3_A2-Pad1B6) -> /RK3562_CORE/A1
- U1 pad 1B8: unconnected-(U1D-AC14/DDR4_A14_WEN/LPDDR4_A4_A/DDR3_A15-Pad1B8) -> /RK3562_CORE/WE_n
- U1 pad A10: unconnected-(U1D-AC2/DDR4_A2/LPDDR4_A1_A/DDR3_A4/LPDDR3_A6-PadA10) -> /RK3562_CORE/A2
- U1 pad A13: unconnected-(U1D-AC23/DDR4_CLK0P/LPDDR4_CLKN_A/DDR3_CLKP/LPDDR3_CLKP-PadA13) -> /RK3562_CORE/CLKP
- U1 pad A15: unconnected-(U1D-AC0/DDR4_A0/LPDDR4_CLKN_B/DDR3_A9-PadA15) -> /RK3562_CORE/A0
- U1 pad A18: unconnected-(U1D-AC6/DDR4_A6/LPDDR4_A1_B/DDR3_A14/LPDDR3_A1-PadA18) -> /RK3562_CORE/A6
- U1 pad A2: unconnected-(U1D-DDR_DM1_A/DDR4_DMU_A/LPDDR4_DM1_A/DDR3_DM1/LPDDR3_DM1-PadA2) -> /RK3562_CORE/DMU
- U1 pad A3: /DDR4_PHY/DQU2 -> /RK3562_CORE/DQU2
- U1 pad A4: /DDR4_PHY/DQU0 -> /RK3562_CORE/DQU0
- U1 pad A6: /DDR4_PHY/DQL7 -> /RK3562_CORE/DQL7
- U1 pad A8: /DDR4_PHY/DQL0 -> /RK3562_CORE/DQL0
- U1 pad B1: /DDR4_PHY/DQU3 -> /RK3562_CORE/DQU3
- U1 pad B10: unconnected-(U1D-AC11/DDR4_A11/LPDDR4_A0_A/DDR3_A6/LPDDR3_A8-PadB10) -> /RK3562_CORE/A11
- U1 pad B11: unconnected-(U1D-AC3/DDR4_A3/LPDDR4_CS0N_A/DDR3_ODT1/LPDDR3_ODT0-PadB11) -> /RK3562_CORE/A3
- U1 pad B12: unconnected-(U1D-AC25/DDR4_CS0N/LPDDR4_CKE1_A/DDR3_A3-PadB12) -> /RK3562_CORE/CS_n
- U1 pad B13: unconnected-(U1D-AC24/DDR4_CLK0N/LPDDR4_CLKP_A/DDR3_CLKN/LPDDR3_CLKN-PadB13) -> /RK3562_CORE/CLKN
- U1 pad B15: unconnected-(U1D-AC9/DDR4_A9/LPDDR4_CLKP_B/DDR3_A13-PadB15) -> /RK3562_CORE/A9
- U1 pad B16: unconnected-(U1D-AC17/DDR4_ACTN/LPDDR4_CKE1_B/DDR3_CASN/LPDDR3_CS1N-PadB16) -> /RK3562_CORE/ACT_n
- U1 pad B18: unconnected-(U1D-AC7/DDR4_A7/LPDDR4_A0_B/DDR3_A5/LPDDR3_A0-PadB18) -> /RK3562_CORE/A7
- U1 pad B19: unconnected-(U1D-AC13/DDR4_A13/LPDDR4_ODT0_CA_B/DDR3_A8/LPDDR3_ODT1-PadB19) -> /RK3562_CORE/A13
- U1 pad B2: /DDR4_PHY/DQU7 -> /RK3562_CORE/DQU7
- U1 pad B3: /DDR4_PHY/DQU6 -> /RK3562_CORE/DQU6
- U1 pad B4: /DDR4_PHY/DQU4 -> /RK3562_CORE/DQU4
- U1 pad B5: /DDR4_PHY/DQL1 -> /RK3562_CORE/DQL1
- U1 pad B6: /DDR4_PHY/DQL6 -> /RK3562_CORE/DQL6
- U1 pad B7: unconnected-(U1D-DDR_DM0_A/DDR4_DML_A/LPDDR4_DM0_A/DDR3_DM0/LPDDR3_DM3-PadB7) -> /RK3562_CORE/DML
- U1 pad B8: /DDR4_PHY/DQL2 -> /RK3562_CORE/DQL2
- U1 pad B9: unconnected-(U1D-AC8/DDR4_A8/LPDDR4_ODT0_CA_A/DDR3_A7/LPDDR3_A9-PadB9) -> /RK3562_CORE/A8
- U1 pad C1: /DDR4_PHY/DQU5 -> /RK3562_CORE/DQU5
- U1 pad C10: unconnected-(U1D-AC15/DDR4_A15_CASN/LPDDR4_A2_A/DDR3_A0/LPDDR3_A7-PadC10) -> /RK3562_CORE/CAS_n
- U1 pad C12: unconnected-(U1D-AC22/DDR4_CKE0/LPDDR4_CKE0_A/DDR3_CKE/LPDDR3_CKE-PadC12) -> /RK3562_CORE/CKE
- U1 pad C16: unconnected-(U1D-AC10/DDR4_A10/LPDDR4_CKE0_B/DDR3_A10/LPDDR3_CS0N-PadC16) -> /RK3562_CORE/A10
- U1 pad C17: unconnected-(U1D-AC27/DDR4_ODT0/LPDDR4_CS1N_B/DDR3_ODT0/LPDDR3_A4-PadC17) -> /RK3562_CORE/ODT
- U1 pad C18: unconnected-(U1D-AC18/DDR4_BA0/LPDDR4_A2_B/DDR3_A1/LPDDR3_A3-PadC18) -> /RK3562_CORE/BA0
- U1 pad C2: /DDR4_PHY/DQU1 -> /RK3562_CORE/DQU1
- U1 pad C5: /DDR4_PHY/DQL5 -> /RK3562_CORE/DQL5
- U1 pad C6: /DDR4_PHY/DQL3 -> /RK3562_CORE/DQL3
- U1 pad C8: /DDR4_PHY/DQL4 -> /RK3562_CORE/DQL4
- U2 pad E2: unconnected-(U2-DMU_n/DBIU_n-PadE2) -> /DDR4_PHY/DMU
- U2 pad E7: unconnected-(U2-DML_n/DBIL_n-PadE7) -> /DDR4_PHY/DML
- U2 pad K2: unconnected-(U2-CKE-PadK2) -> /DDR4_PHY/CKE
- U2 pad K3: unconnected-(U2-ODT-PadK3) -> /DDR4_PHY/ODT
- U2 pad K7: unconnected-(U2-CK_t-PadK7) -> /DDR4_PHY/CLKP
- U2 pad K8: unconnected-(U2-CK_c-PadK8) -> /DDR4_PHY/CLKN
- U2 pad L2: unconnected-(U2-WE_n/A14-PadL2) -> /DDR4_PHY/WE_n
- U2 pad L3: unconnected-(U2-ACT_n-PadL3) -> /DDR4_PHY/ACT_n
- U2 pad L7: unconnected-(U2-CS_n-PadL7) -> /DDR4_PHY/CS_n
- U2 pad L8: unconnected-(U2-RAS_n/A16-PadL8) -> /DDR4_PHY/RAS_n
- U2 pad M2: unconnected-(U2-BG0-PadM2) -> /DDR4_PHY/BG0
- U2 pad M3: unconnected-(U2-A10/AP-PadM3) -> /DDR4_PHY/A10
- U2 pad M7: unconnected-(U2-A12/BC_n-PadM7) -> /DDR4_PHY/A12
- U2 pad M8: unconnected-(U2-CAS_n/A15-PadM8) -> /DDR4_PHY/CAS_n
- U2 pad N2: unconnected-(U2-BA0-PadN2) -> /DDR4_PHY/BA0
- U2 pad N3: unconnected-(U2-A4-PadN3) -> /DDR4_PHY/A4
- U2 pad N7: unconnected-(U2-A3-PadN7) -> /DDR4_PHY/A3
- U2 pad N8: unconnected-(U2-BA1-PadN8) -> /DDR4_PHY/BA1
- U2 pad P1: unconnected-(U2-RESET_n-PadP1) -> /DDR4_PHY/RESET_n
- U2 pad P2: unconnected-(U2-A6-PadP2) -> /DDR4_PHY/A6
- U2 pad P3: unconnected-(U2-A0-PadP3) -> /DDR4_PHY/A0
- U2 pad P7: unconnected-(U2-A1-PadP7) -> /DDR4_PHY/A1
- U2 pad P8: unconnected-(U2-A5-PadP8) -> /DDR4_PHY/A5
- U2 pad R2: unconnected-(U2-A8-PadR2) -> /DDR4_PHY/A8
- U2 pad R3: unconnected-(U2-A2-PadR3) -> /DDR4_PHY/A2
- U2 pad R7: unconnected-(U2-A9-PadR7) -> /DDR4_PHY/A9
- U2 pad R8: unconnected-(U2-A7-PadR8) -> /DDR4_PHY/A7
- U2 pad T2: unconnected-(U2-A11-PadT2) -> /DDR4_PHY/A11
- U2 pad T8: unconnected-(U2-A13-PadT8) -> /DDR4_PHY/A13
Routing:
- net GND: vias 0 -> 1
- net +1V2: vias 0 -> 1

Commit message: New SoC
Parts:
- removed C1, C10, C11, C12, C13, C14, C15, C16, C17, C18, C19, C2, C20, C3, C4, C5, C6, C7, C8, C9: 100n, Capacitor_SMD:C_0201_0603Metric
- removed U2: FJBD4N8GT6L9-SKC, easyeda2kicad:FBGA-96_L14.0-W9.0-R16-C6-P0.80-TL
- U1: value RK3562 -> NT5CB256M16ER-FL; footprint Package_BGA:RK3562 -> Package_BGA:FBGA-96_8x13mm_Layout9x16_P0.8mm
- moved U1 18.2 mm to (150.8, 90.7), turned to 90 degrees
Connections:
- U1 pad A1: GND -> unconnected-(U1-VDDQ-PadA1)
- U1 pad A2: /RK3562_CORE/DMU -> unconnected-(U1-DQU5-PadA2)
- U1 pad A3: /RK3562_CORE/DQU2 -> unconnected-(U1-DQU7-PadA3)
- U1 pad A8: /RK3562_CORE/DQL0 -> unconnected-(U1-VDDQ-PadA8)
- U1 pad B1: /RK3562_CORE/DQU3 -> unconnected-(U1-VSSQ-PadB1)
- U1 pad B2: /RK3562_CORE/DQU7 -> unconnected-(U1-VDD-PadB2)
- U1 pad B3: /RK3562_CORE/DQU6 -> unconnected-(U1-VSS-PadB3)
- U1 pad B7: /RK3562_CORE/DML -> unconnected-(U1-~{DQSU}-PadB7)
- U1 pad B8: /RK3562_CORE/DQL2 -> unconnected-(U1-DQU6-PadB8)
- U1 pad B9: /RK3562_CORE/A8 -> unconnected-(U1-VSSQ-PadB9)
- U1 pad C1: /RK3562_CORE/DQU5 -> unconnected-(U1-VDDQ-PadC1)
- U1 pad C2: /RK3562_CORE/DQU1 -> unconnected-(U1-DQU3-PadC2)
- U1 pad C3: GND -> unconnected-(U1-DQU1-PadC3)
- U1 pad C7: GND -> unconnected-(U1-DQSU-PadC7)
- U1 pad C8: /RK3562_CORE/DQL4 -> unconnected-(U1-DQU2-PadC8)
- U1 pad C9: GND -> unconnected-(U1-VDDQ-PadC9)
- U1 pad D2: GND -> unconnected-(U1-VDDQ-PadD2)
- U1 pad E3: GND -> unconnected-(U1-DQL0-PadE3)
- U1 pad F3: GND -> unconnected-(U1-DQSL-PadF3)
- U1 pad J3: GND -> unconnected-(U1-~{RAS}-PadJ3)
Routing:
- net GND: vias 1 -> 0
- net +1V2: vias 1 -> 0
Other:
- board outline removed
- copper layers 2 -> 6
